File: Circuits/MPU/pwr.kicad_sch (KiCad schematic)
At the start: 97 parts, among them Q7 MMBT2222A, Q8 MMBT2222A, T1 HPH1-1400L, U1 ProASIC, U16 DG403, U17 REF43GS, U18 ADA4805-2ARMZ, U19 ADA4805-2ARMZ

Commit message: Values for TBD caps
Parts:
- C46, C47, C48: value TBD -> 10uF; Spec 16WVDC X7R -> 50WVDC X7R
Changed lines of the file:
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@@
 			)
 		)
-		(property "Value" "TBD"
+		(property "Value" "10uF"
 			(at 109.22 129.5399 0)
 			(effects
@@
 			)
 		)
-		(property "Spec" "16WVDC X7R"
+		(property "Spec" "50WVDC X7R"
 			(at 105.41 128.27 0)
 			(effects
@@
 			)
 		)
-		(property "Value" "TBD"
+		(property "Value" "10uF"
 			(at 113.03 167.6399 0)
 			(effects
@@
 			)
 		)
-		(property "Spec" "16WVDC X7R"
+		(property "Spec" "50WVDC X7R"
 			(at 109.22 166.37 0)
 			(effects
@@
 			)
 		)
-		(property "Value" "TBD"
+		(property "Value" "10uF"
 			(at 113.03 191.7699 0)
 			(effects
@@
 			)
 		)
-		(property "Spec" "16WVDC X7R"
+		(property "Spec" "50WVDC X7R"
 			(at 109.22 190.5 0)
 			(effects

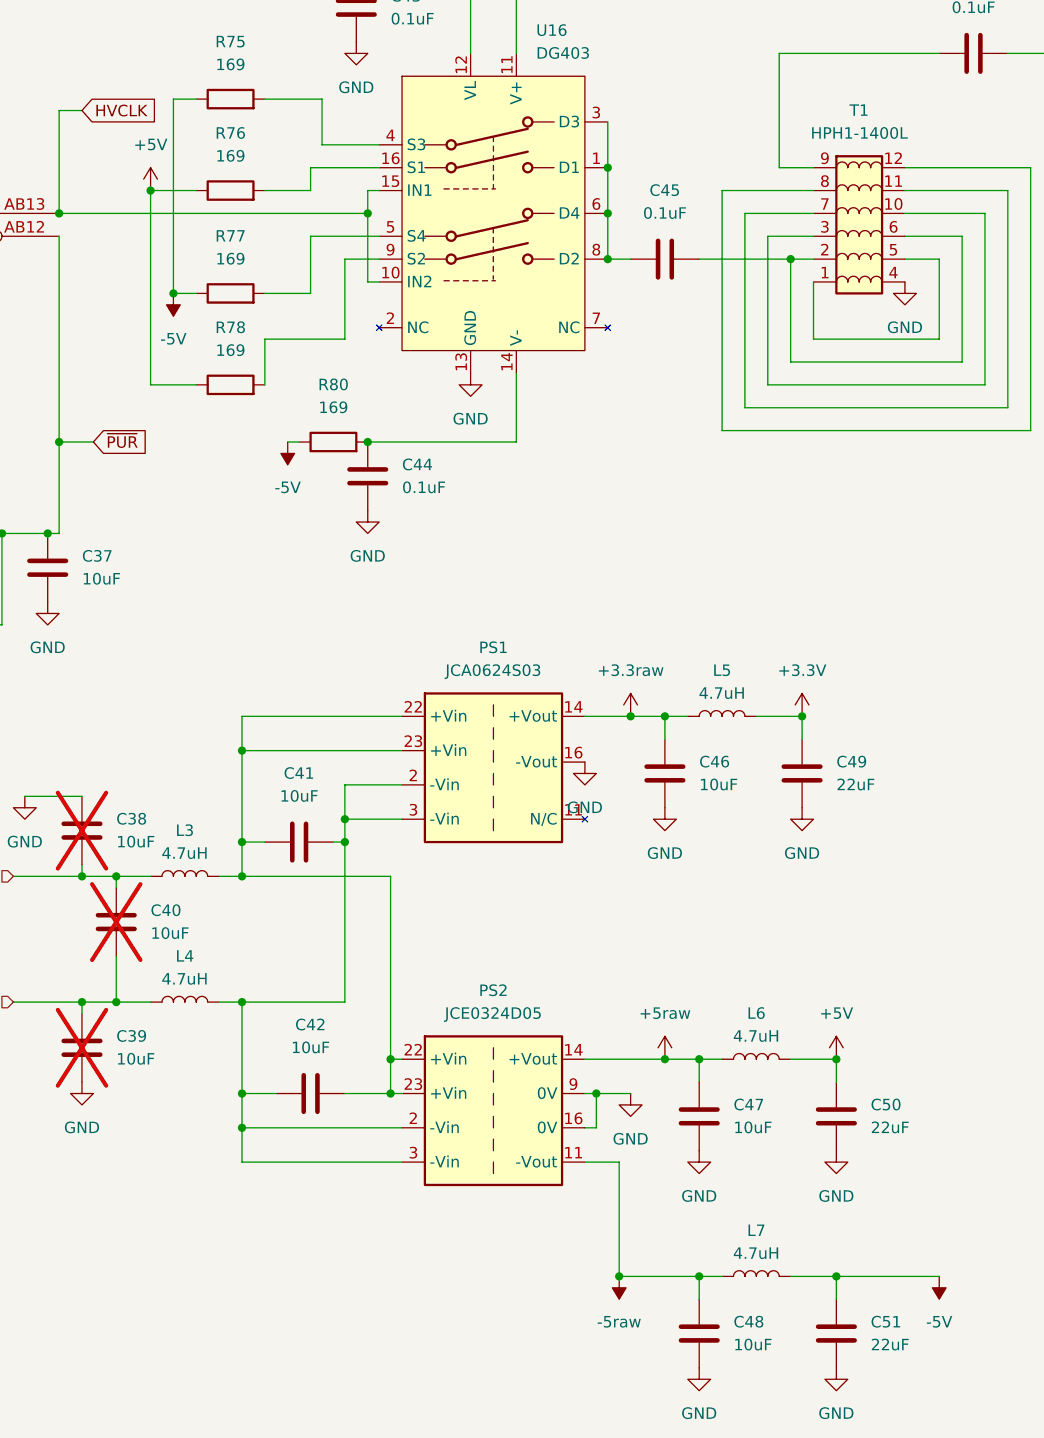
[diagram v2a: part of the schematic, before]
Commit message: Files changed due to KiCAD update
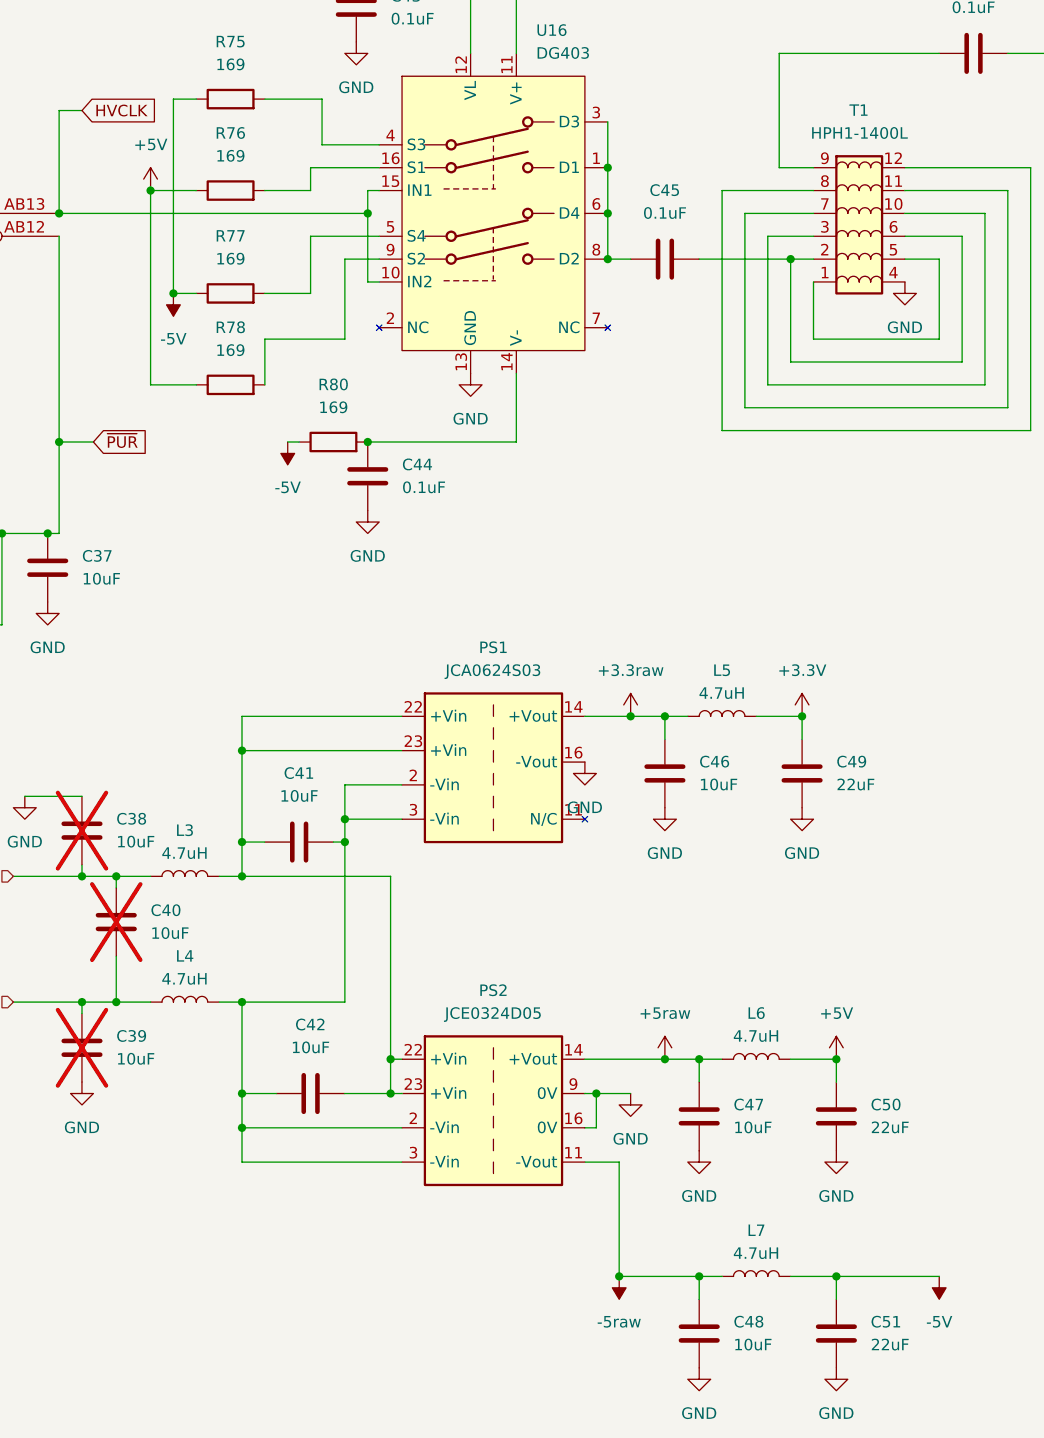
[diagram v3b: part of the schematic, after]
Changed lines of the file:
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@@
 (kicad_sch
-	(version 20231120)
+	(version 20250114)
 	(generator "eeschema")
-	(generator_version "8.0")
+	(generator_version "9.0")
 	(paper "USLetter")
 	(title_block
@@
 		(shape input)
 		(at 33.02 153.67 180)
-		(fields_autoplaced yes)
 		(effects
 			(font
@@
 		(shape input)
 		(at 33.02 139.7 180)
-		(fields_autoplaced yes)
 		(effects
 			(font

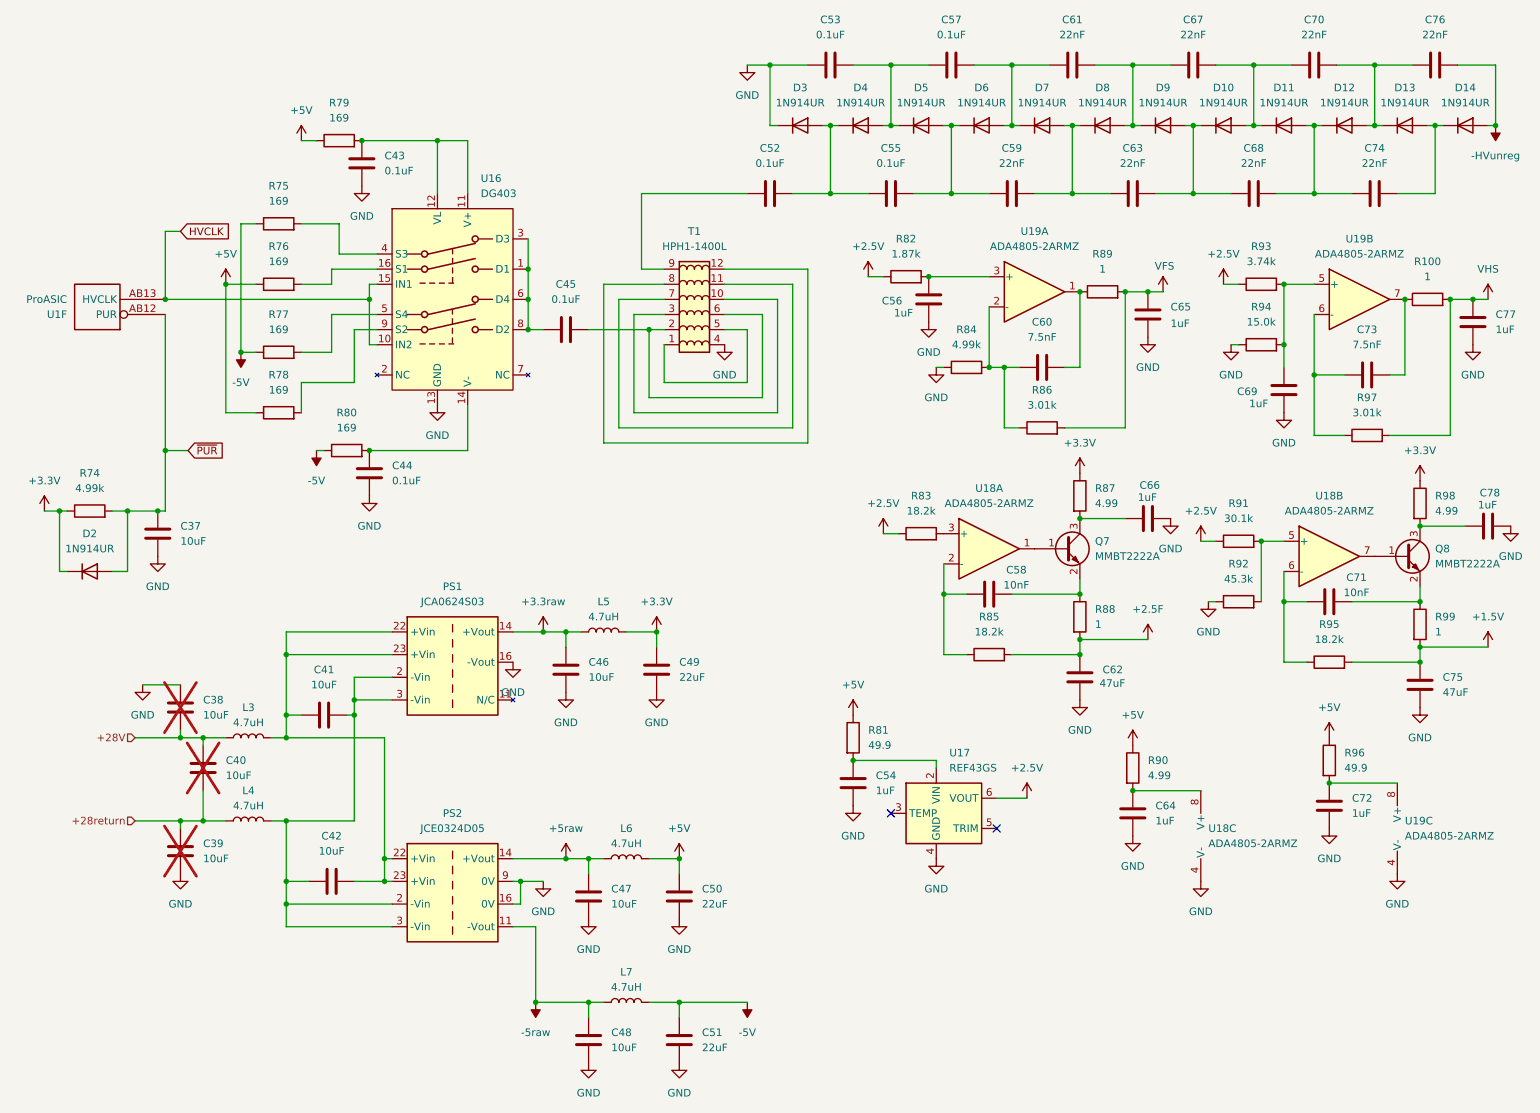
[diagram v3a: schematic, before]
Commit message: S/H for fast channel. Higher HV.
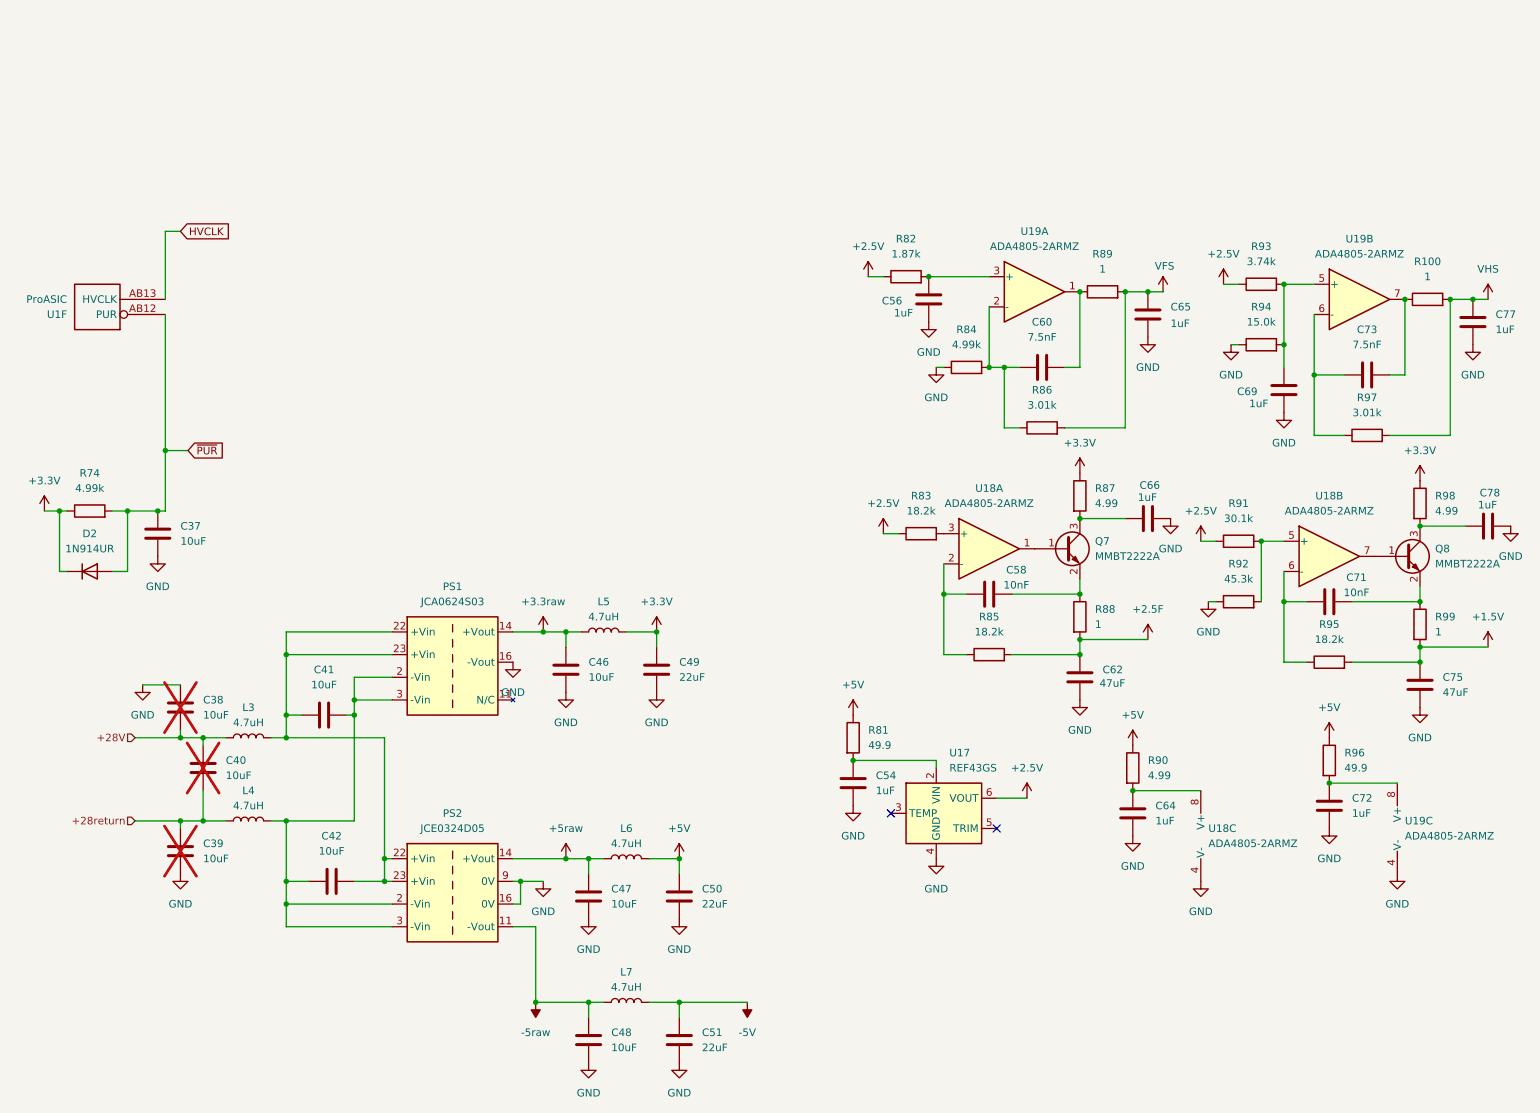
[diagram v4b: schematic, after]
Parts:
- removed C43, C44: 0.1uF, Capacitor_SMD:C_0603_1608Metric, symbol QuERI_symbols:Csmall
- removed C45, C52, C53, C55, C57: 0.1uF, Capacitor_SMD:C_0603_1608Metric, symbol QuERI_symbols:C
- removed C59, C61, C63, C67, C68, C70, C74, C76: 22nF, Capacitor_SMD:C_0603_1608Metric, symbol QuERI_symbols:Csmall
- removed D10, D11, D12, D13, D14, D3, D4, D5, D6, D7, D8, D9: 1N914UR, Diode_SMD:D_MiniMELF, symbol QuERI_symbols:1N914UR
- removed R75, R76, R77, R78, R79, R80: 169, Resistor_SMD:R_1206_3216Metric, symbol Device:R
- removed T1: HPH1-1400L, symbol QuERI_symbols:Hexapath
- removed U16: DG403, Package_SO:SOIC-16_3.9x9.9mm_P1.27mm, symbol QuERI_symbols:DG403
